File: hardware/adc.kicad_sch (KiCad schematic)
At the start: 6 parts, among them U2 AD8603

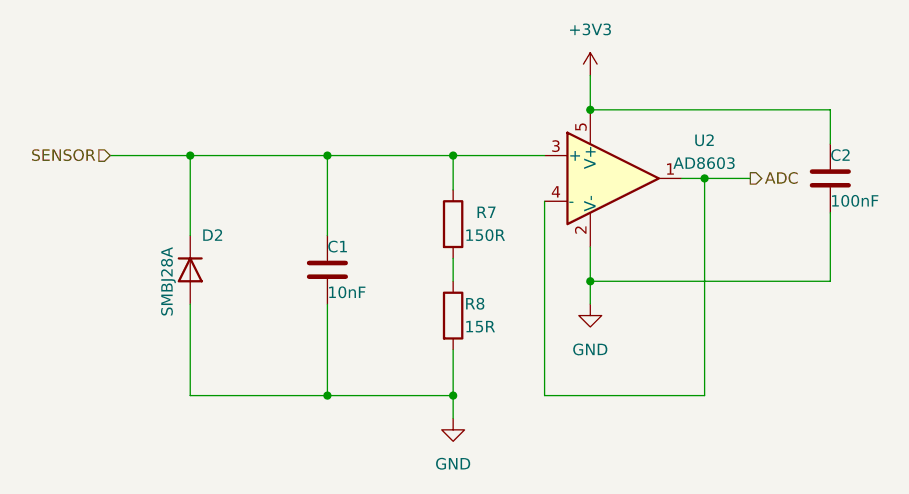
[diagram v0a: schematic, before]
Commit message: * 3V8 Power design fixed * Footprints assigned * Bom exported * PCB filter module placed
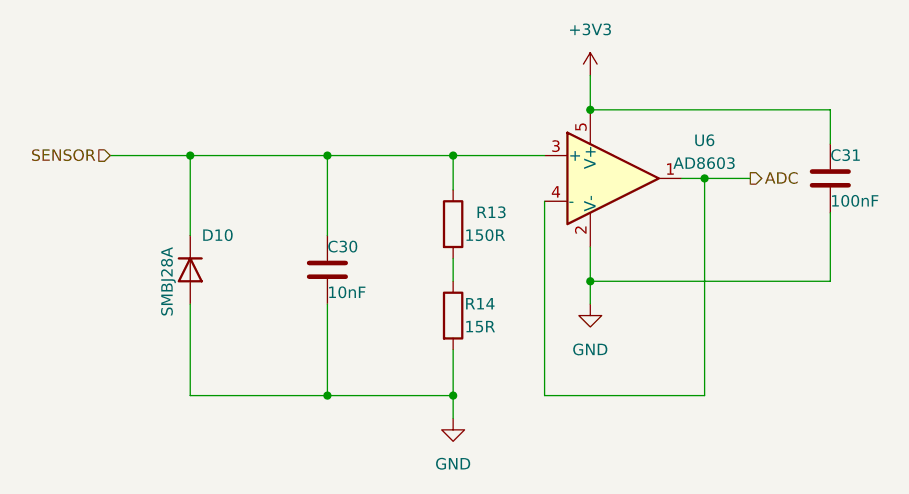
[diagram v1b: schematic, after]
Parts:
- C30: renamed from C1; footprint (none) -> Capacitor_SMD:C_0603_1608Metric
- C31: renamed from C2; footprint (none) -> Capacitor_SMD:C_0603_1608Metric
- R13: renamed from R7; footprint (none) -> Resistor_SMD:R_0603_1608Metric
- R14: renamed from R8; footprint (none) -> Resistor_SMD:R_0603_1608Metric
- renumbered D2 to D10, U2 to U6
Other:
- company: (none) -> Hidro Elektronik
- title: (none) -> 2023 Staj Projesi
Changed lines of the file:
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@@
 (kicad_sch (version 20230121) (generator eeschema)
   (paper "A4")
+  (title_block
+    (title "2023 Staj Projesi")
+    (date "2023-07-24")
+    (rev "1.0")
+    (company "Hidro Elektronik")
+    (comment 1 "Mehmet Emre SAYGI(2019513057@ogr.cu.edu.tr)")
+    (comment 2 "Yilmaz Can DURAN(duranyilmazcan@gmail.com)")
+    (comment 3 "Asli VEZIR(vezirasli@gmail.com)")
+  )
   (junction (at 152.4 73.66) (diameter 0) (color 0 0 0 0)
   )
@@
   (symbol (lib_id "Device:C") (at 179.07 81.28 0) (unit 1)
     (in_bom yes) (on_board yes) (dnp no)
-    (property "Reference" "C2" (at 179.07 78.74 0)
+    (property "Reference" "C31" (at 179.07 78.74 0)
       (effects (font (size 1.27 1.27)) (justify left))
     )
@@
       (effects (font (size 1.27 1.27)) (justify left))
     )
-    (property "Footprint" "" (at 180.0352 85.09 0)
+    (property "Footprint" "Capacitor_SMD:C_0603_1608Metric" (at 180.0352 85.09 0)
       (effects (font (size 1.27 1.27)) hide)
     )
@@
       (project "2023-staj-projesi"
         (path "/069db7ad-35cd-4aa8-8111-e026f632a4df/4fc35e70-cee4-4196-a30c-3982173d08bb"
-          (reference "C2") (unit 1)
+          (reference "C31") (unit 1)
         )
       )
@@
   (symbol (lib_id "Device:R") (at 137.16 86.36 0) (unit 1)
     (in_bom yes) (on_board yes) (dnp no)
-    (property "Reference" "R7" (at 139.7 85.09 0)
+    (property "Reference" "R13" (at 139.7 85.09 0)
       (effects (font (size 1.27 1.27)) (justify left))
     )
@@
       (effects (font (size 1.27 1.27)) (justify left))
     )
-    (property "Footprint" "" (at 135.382 86.36 90)
+    (property "Footprint" "Resistor_SMD:R_0603_1608Metric" (at 135.382 86.36 90)
       (effects (font (size 1.27 1.27)) hide)
     )
@@
       (project "2023-staj-projesi"
         (path "/069db7ad-35cd-4aa8-8111-e026f632a4df/4fc35e70-cee4-4196-a30c-3982173d08bb"
-          (reference "R7") (unit 1)
+          (reference "R13") (unit 1)
         )
       )
@@
   (symbol (lib_id "power:GND") (at 152.4 95.25 0) (unit 1)
     (in_bom yes) (on_board yes) (dnp no) (fields_autoplaced)
-    (property "Reference" "#PWR06" (at 152.4 101.6 0)
+    (property "Reference" "#PWR042" (at 152.4 101.6 0)
       (effects (font (size 1.27 1.27)) hide)
     )
@@
       (project "2023-staj-projesi"
         (path "/069db7ad-35cd-4aa8-8111-e026f632a4df/4fc35e70-cee4-4196-a30c-3982173d08bb"
-          (reference "#PWR06") (unit 1)
+          (reference "#PWR042") (unit 1)
         )
       )
@@
   (symbol (lib_id "Amplifier_Operational:AD8603") (at 154.94 81.28 0) (unit 1)
     (in_bom yes) (on_board yes) (dnp no) (fields_autoplaced)
-    (property "Reference" "U2" (at 165.1 77.0891 0)
+    (property "Reference" "U6" (at 165.1 77.0891 0)
       (effects (font (size 1.27 1.27)))
     )
@@
       (project "2023-staj-projesi"
         (path "/069db7ad-35cd-4aa8-8111-e026f632a4df/4fc35e70-cee4-4196-a30c-3982173d08bb"
-          (reference "U2") (unit 1)
+          (reference "U6") (unit 1)
         )
       )
@@
   (symbol (lib_id "Diode:1N914") (at 107.95 91.44 270) (unit 1)
     (in_bom yes) (on_board yes) (dnp no)
-    (property "Reference" "D2" (at 109.22 87.63 90)
+    (property "Reference" "D10" (at 109.22 87.63 90)
       (effects (font (size 1.27 1.27)) (justify left))
     )
@@
       (project "2023-staj-projesi"
         (path "/069db7ad-35cd-4aa8-8111-e026f632a4df/4fc35e70-cee4-4196-a30c-3982173d08bb"
-          (reference "D2") (unit 1)
+          (reference "D10") (unit 1)
         )
       )
@@
   (symbol (lib_id "Device:R") (at 137.16 96.52 0) (unit 1)
     (in_bom yes) (on_board yes) (dnp no)
-    (property "Reference" "R8" (at 138.43 95.25 0)
+    (property "Reference" "R14" (at 138.43 95.25 0)
       (effects (font (size 1.27 1.27)) (justify left))
     )
@@
       (effects (font (size 1.27 1.27)) (justify left))
     )
-    (property "Footprint" "" (at 135.382 96.52 90)
+    (property "Footprint" "Resistor_SMD:R_0603_1608Metric" (at 135.382 96.52 90)
       (effects (font (size 1.27 1.27)) hide)
     )
@@
       (project "2023-staj-projesi"
         (path "/069db7ad-35cd-4aa8-8111-e026f632a4df/4fc35e70-cee4-4196-a30c-3982173d08bb"
-          (reference "R8") (unit 1)
+          (reference "R14") (unit 1)
         )
       )
@@
   (symbol (lib_id "power:+3V3") (at 152.4 69.85 0) (unit 1)
     (in_bom yes) (on_board yes) (dnp no) (fields_autoplaced)
-    (property "Reference" "#PWR05" (at 152.4 73.66 0)
+    (property "Reference" "#PWR041" (at 152.4 73.66 0)
       (effects (font (size 1.27 1.27)) hide)
     )
@@
       (project "2023-staj-projesi"
         (path "/069db7ad-35cd-4aa8-8111-e026f632a4df/4fc35e70-cee4-4196-a30c-3982173d08bb"
-          (reference "#PWR05") (unit 1)
+          (reference "#PWR041") (unit 1)
         )
       )
@@
   (symbol (lib_id "power:GND") (at 137.16 107.95 0) (unit 1)
     (in_bom yes) (on_board yes) (dnp no) (fields_autoplaced)
-    (property "Reference" "#PWR08" (at 137.16 114.3 0)
+    (property "Reference" "#PWR040" (at 137.16 114.3 0)
       (effects (font (size 1.27 1.27)) hide)
     )
@@
       (project "2023-staj-projesi"
         (path "/069db7ad-35cd-4aa8-8111-e026f632a4df/4fc35e70-cee4-4196-a30c-3982173d08bb"
-          (reference "#PWR08") (unit 1)
+          (reference "#PWR040") (unit 1)
         )
       )
@@
   (symbol (lib_id "Device:C") (at 123.19 91.44 0) (unit 1)
     (in_bom yes) (on_board yes) (dnp no)
-    (property "Reference" "C1" (at 123.19 88.9 0)
+    (property "Reference" "C30" (at 123.19 88.9 0)
       (effects (font (size 1.27 1.27)) (justify left))
     )
@@
       (effects (font (size 1.27 1.27)) (justify left))
     )
-    (property "Footprint" "" (at 124.1552 95.25 0)
+    (property "Footprint" "Capacitor_SMD:C_0603_1608Metric" (at 124.1552 95.25 0)
       (effects (font (size 1.27 1.27)) hide)
     )
@@
       (project "2023-staj-projesi"
         (path "/069db7ad-35cd-4aa8-8111-e026f632a4df/4fc35e70-cee4-4196-a30c-3982173d08bb"
-          (reference "C1") (unit 1)
-        )
-      )
+          (reference "C30") (unit 1)
+        )
+      )
